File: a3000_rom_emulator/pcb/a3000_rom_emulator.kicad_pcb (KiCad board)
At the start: 4 copper layers, 43.2 x 78.7 mm, 43 parts

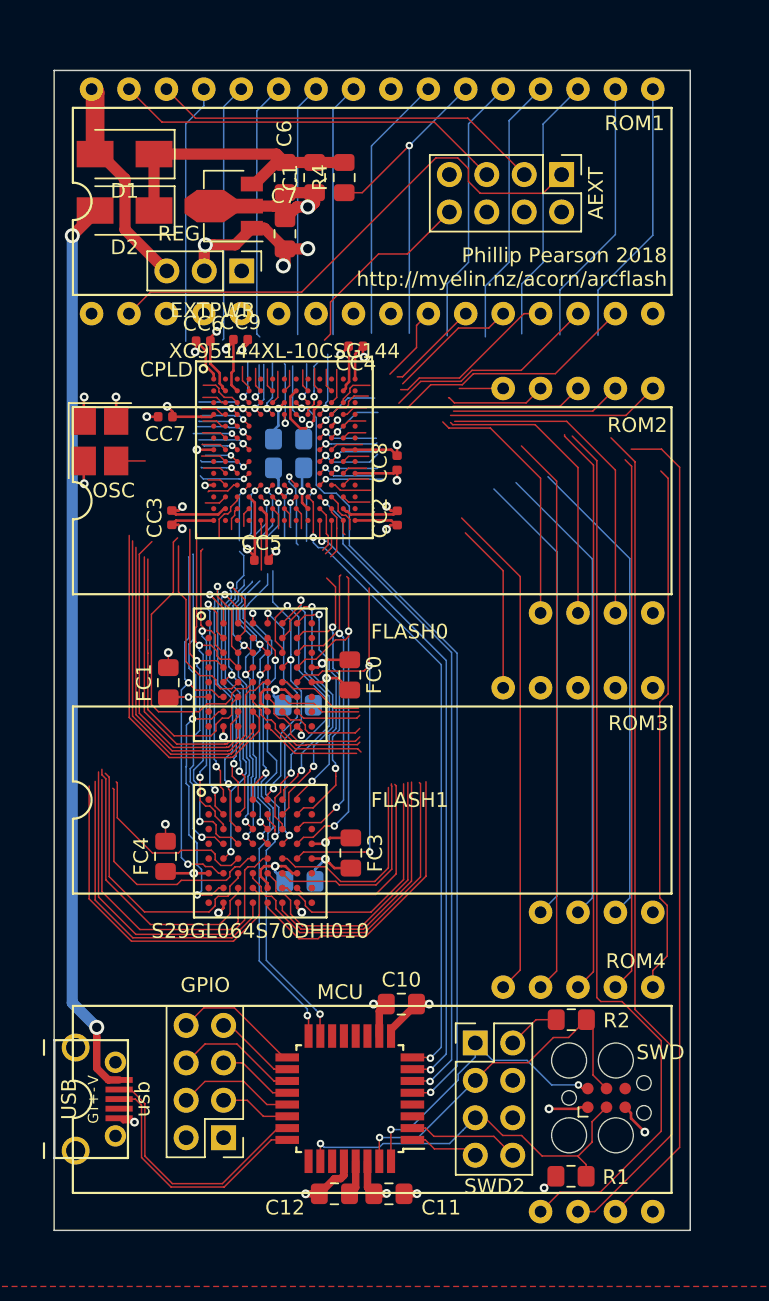
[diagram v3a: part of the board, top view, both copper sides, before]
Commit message: CPLD partially routed
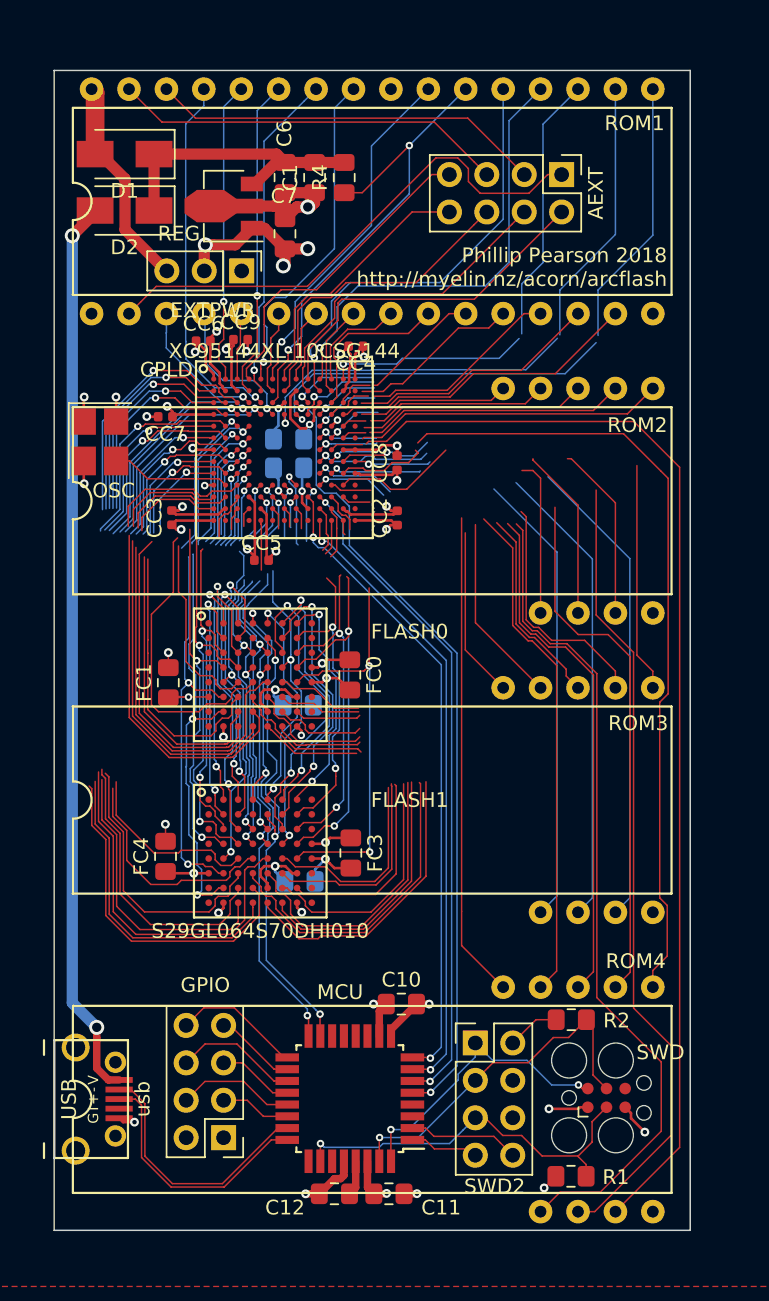
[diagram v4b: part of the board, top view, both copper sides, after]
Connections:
- CPLD pad A10: dummy_A10 -> rom_D6
- CPLD pad A11: dummy_A11 -> rom_A3
- CPLD pad A2: arc_RESET -> rom_A13
- CPLD pad A3: dummy_A3 -> rom_A7
- CPLD pad A4: dummy_A4 -> rom_A19
- CPLD pad A5: dummy_A5 -> rom_A11
- CPLD pad A6: dummy_A6 -> rom_A10
- CPLD pad A7: dummy_A7 -> arc_RESET
- CPLD pad A8: dummy_A8 -> rom_A5
- CPLD pad A9: dummy_A9 -> rom_A16
- CPLD pad B10: dummy_B10 -> rom_D7
- CPLD pad B11: dummy_B11 -> rom_A4
- CPLD pad B4: dummy_B4 -> rom_A8
- CPLD pad B5: dummy_B5 -> rom_A9
- CPLD pad B6: dummy_B6 -> rom_A6
- CPLD pad B7: dummy_B7 -> rom_A18
- CPLD pad B9: dummy_B9 -> rom_A17
- CPLD pad C11: dummy_C11 -> rom_A2
- CPLD pad C4: dummy_C4 -> rom_A15
- CPLD pad C5: dummy_C5 -> rom_A14
- CPLD pad C6: dummy_C6 -> rom_nCS
- CPLD pad D6: dummy_D6 -> rom_A12
- CPLD pad K2: dummy_K2_GCK1 -> osc_output
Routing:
- net rom_A16: track 0.00 -> 23.7 mm
- net rom_A17: track 0.00 -> 22.5 mm
- net rom_A19: track 0.00 -> 21.8 mm
- net rom_A18: track 0.00 -> 21.4 mm
- net dummy_D8: track 4.45 -> 24.5 mm
- net rom_D26: track 56.1 -> 75.5 mm
- net dummy_D7: track 4.69 -> 22.5 mm
- net rom_D27: track 36.1 -> 53.9 mm
- net rom_D20: track 0.00 -> 16.1 mm
- net rom_D19: track 0.00 -> 15.5 mm
- net dummy_B1: track 0.00 -> 14.8 mm, vias 0 -> 1
- net dummy_C3: track 2.94 -> 17.6 mm, vias 0 -> 1
- net rom_D21: track 0.00 -> 13.7 mm
- net dummy_A12: track 0.00 -> 13.7 mm, vias 0 -> 1
- net dummy_C1: track 0.00 -> 13.7 mm, vias 0 -> 1
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
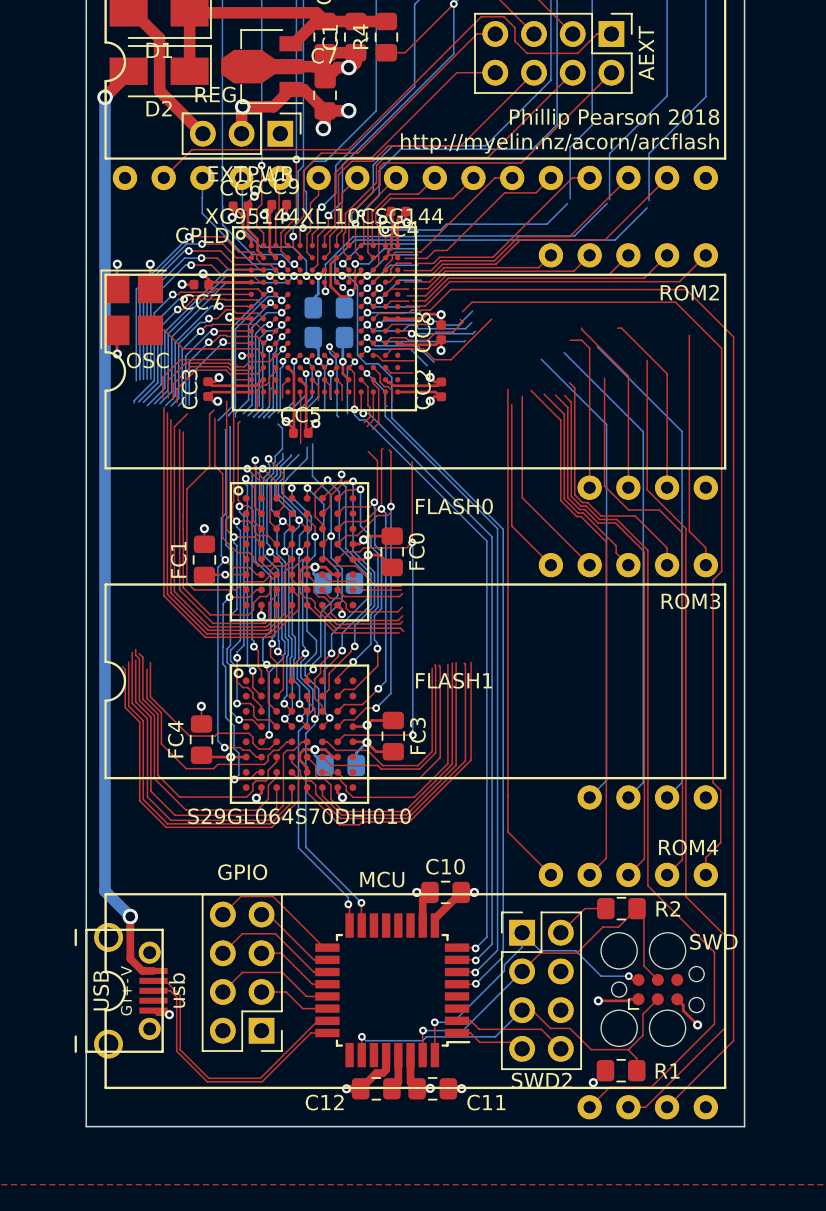
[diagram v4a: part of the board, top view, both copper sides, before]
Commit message: Fully routed PCB (still needs tidying) and basic Verilog for a3000_rom_emulator
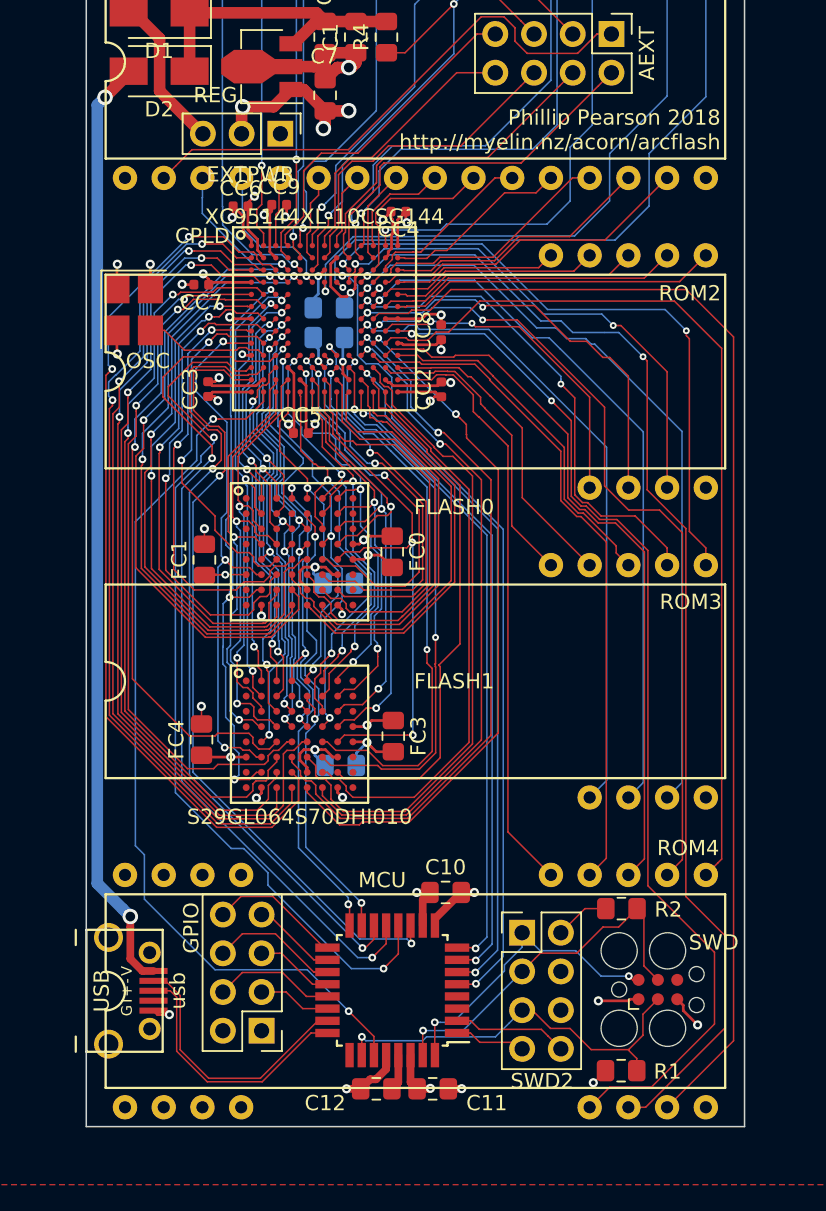
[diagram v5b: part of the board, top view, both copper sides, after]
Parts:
- added mech_pin1: , myelin-kicad:dip_rom_single_pin, F.Cu at (142.2, 91.4)
- added mech_pin2: , myelin-kicad:dip_rom_single_pin, F.Cu at (144.8, 91.4)
- added mech_pin3: , myelin-kicad:dip_rom_single_pin, F.Cu at (147.3, 91.4)
- added mech_pin4: , myelin-kicad:dip_rom_single_pin, F.Cu at (149.9, 91.4)
- added mech_pin5: , myelin-kicad:dip_rom_single_pin, F.Cu at (142.2, 106.7)
- added mech_pin6: , myelin-kicad:dip_rom_single_pin, F.Cu at (144.8, 106.7)
- added mech_pin7: , myelin-kicad:dip_rom_single_pin, F.Cu at (147.3, 106.7)
- added mech_pin8: , myelin-kicad:dip_rom_single_pin, F.Cu at (149.9, 106.7)
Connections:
- net osc_output renamed cpld_clock_osc
- CPLD pad A12: dummy_A12 -> rom_D5
- CPLD pad B1: dummy_B1 -> flash1_DQ3
- CPLD pad B13: dummy_B13 -> rom_A0
- CPLD pad C1: dummy_C1 -> flash1_DQ1
- CPLD pad C12: dummy_C12 -> rom_A1
- CPLD pad C13: dummy_C13 -> rom_D1
- CPLD pad C2: dummy_C2 -> flash1_DQ5
- CPLD pad C3: dummy_C3 -> flash1_DQ11
- CPLD pad C9: dummy_C9 -> rom_D19
- CPLD pad D10: dummy_D10 -> rom_D25
- CPLD pad D11: dummy_D11 -> rom_D0
- CPLD pad D12: dummy_D12 -> rom_D2
- CPLD pad D13: dummy_D13 -> rom_D15
- CPLD pad D2: dummy_D2 -> flash1_DQ9
- CPLD pad D3: dummy_D3 -> flash0_DQ3
- CPLD pad D4: dummy_D4 -> flash0_DQ11
- CPLD pad D5: dummy_D5 -> flash0_DQ5
- CPLD pad D7: dummy_D7 -> rom_D4
- CPLD pad D8: dummy_D8 -> rom_D3
- CPLD pad D9: dummy_D9 -> rom_D10
- CPLD pad E1: dummy_E1 -> flash1_DQ2
- CPLD pad E10: dummy_E10 -> rom_D18
- CPLD pad E12: dummy_E12 -> rom_D14
- CPLD pad E13: dummy_E13 -> rom_D13
- CPLD pad E2: dummy_E2 -> flash1_DQ8
- CPLD pad E3: dummy_E3 -> flash_nOE
- CPLD pad E4: dummy_E4 -> flash_A4
- CPLD pad F1: dummy_F1 -> flash0_DQ1
- CPLD pad F10: dummy_F10 -> rom_D20
- CPLD pad F11: dummy_F11 -> rom_D17
- CPLD pad F12: dummy_F12 -> rom_D12
- CPLD pad F13: dummy_F13 -> rom_D11
- CPLD pad F2: dummy_F2 -> flash1_DQ0
- CPLD pad F3: dummy_F3 -> flash_A3
- CPLD pad F4: dummy_F4 -> flash_A6
- CPLD pad G10: dummy_G10 -> rom_D9
- CPLD pad G11: dummy_G11 -> rom_D26
- CPLD pad G2: dummy_G2 -> flash0_DQ9
- CPLD pad G3: dummy_G3 -> flash_A7
- CPLD pad G4: dummy_G4 -> flash_A0
- CPLD pad H1: dummy_H1 -> flash0_DQ2
- CPLD pad H10: dummy_H10 -> rom_D16
- CPLD pad H11: dummy_H11 -> rom_D28
- CPLD pad H12: dummy_H12 -> rom_D8
- CPLD pad H13: dummy_H13 -> rom_D24
- CPLD pad H2: dummy_H2 -> flash0_DQ8
- CPLD pad H3: dummy_H3 -> flash_A18
- CPLD pad H4: dummy_H4 -> flash_A21
- CPLD pad J1: dummy_J1 -> flash_nCE
- CPLD pad J10: dummy_J10 -> flash1_DQ10
- CPLD pad J11: dummy_J11 -> flash1_DQ4
- CPLD pad J12: dummy_J12 -> rom_D27
- CPLD pad J2: dummy_J2 -> flash0_DQ0
- CPLD pad J3: dummy_J3 -> flash_A20
- CPLD pad J4: dummy_J4 -> flash_A19
- CPLD pad K10: dummy_K10 -> flash1_DQ6
- CPLD pad K11: dummy_K11 -> rom_D30
- CPLD pad K12: dummy_K12 -> rom_D29
- CPLD pad K13: dummy_K13 -> rom_D21
- CPLD pad K3: dummy_K3 -> cpld_SS
- CPLD pad K4: dummy_K4 -> flash_A11
- CPLD pad K5: dummy_K5 -> flash_A9
- CPLD pad K6: dummy_K6 -> flash_A14
- CPLD pad K7: dummy_K7 -> flash0_DQ14
- CPLD pad K8: dummy_K8 -> flash1_DQ7
- CPLD pad K9: dummy_K9 -> flash1_DQ14
- CPLD pad L1: dummy_L1_GCK2 -> cpld_SCK
- CPLD pad L11: dummy_L11 -> flash1_DQ12
- CPLD pad L12: dummy_L12 -> rom_D23
- CPLD pad L13: dummy_L13 -> rom_D22
- CPLD pad L2: dummy_L2 -> cpld_MISO
- CPLD pad L3: dummy_L3 -> flash_A17
- CPLD pad L5: dummy_L5 -> flash_A13
- CPLD pad L6: dummy_L6 -> flash0_DQ7
- CPLD pad L8: dummy_L8 -> flash0_DQ15
- CPLD pad M1: dummy_M1 -> cpld_MOSI
- CPLD pad M10: dummy_M10 -> flash0_DQ10
- CPLD pad M11: dummy_M11 -> flash1_DQ15
- CPLD pad M13: dummy_M13 -> rom_D31
- CPLD pad M3: dummy_M3 -> flash_A1
- CPLD pad M4: dummy_M4 -> flash_A2
- CPLD pad M6: dummy_M6 -> flash_A12
- CPLD pad M7: dummy_M7 -> flash_A16
- CPLD pad M8: dummy_M8 -> flash0_DQ12
- CPLD pad N11: dummy_N11 -> flash0_DQ4
- CPLD pad N12: dummy_N12 -> flash1_DQ13
- CPLD pad N2: dummy_N2_GCK3 -> cpld_clock_from_mcu
- CPLD pad N3: dummy_N3 -> flash_A5
- CPLD pad N4: dummy_N4 -> flash_nWE
- CPLD pad N5: dummy_N5 -> flash_A10
- CPLD pad N6: dummy_N6 -> flash_A8
- CPLD pad N7: dummy_N7 -> flash_A15
- CPLD pad N8: dummy_N8 -> flash0_DQ13
- CPLD pad N9: dummy_N9 -> flash0_DQ6
- MCU pad 27: (no net) -> cpld_clock_from_mcu
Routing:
- net cpld_clock_from_mcu: track 0.00 -> 58.3 mm, vias 0 -> 2
- net cpld_SCK: track 0.00 -> 57.6 mm, vias 0 -> 2
- net cpld_SS: track 0.00 -> 56.7 mm, vias 0 -> 2
- net cpld_MOSI: track 0.00 -> 52.6 mm, vias 0 -> 2
- net cpld_MISO: track 0.00 -> 51.9 mm, vias 0 -> 2
- net flash1_DQ11: track 23.2 -> 59.1 mm, vias 0 -> 2
- net flash1_DQ3: track 21.4 -> 54.3 mm, vias 0 -> 2
- net flash1_DQ5: track 25.1 -> 57.7 mm, vias 0 -> 2
- net flash1_DQ1: track 19.4 -> 51.1 mm, vias 0 -> 2
- net flash1_DQ9: track 19.6 -> 51.2 mm, vias 0 -> 2
- net flash1_DQ2: track 15.5 -> 46.4 mm, vias 0 -> 2
- net flash1_DQ0: track 12.5 -> 43.5 mm, vias 0 -> 2
- net flash1_DQ8: track 18.7 -> 49.1 mm, vias 0 -> 2
- net rom_D19: track 15.5 -> 41.9 mm, vias 0 -> 2
- net flash1_DQ10: track 21.8 -> 48.0 mm, vias 0 -> 2
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
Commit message: Tidy up some traces
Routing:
- net rom_D7: track 29.7 -> 26.2 mm
- net rom_D6: track 31.1 -> 28.5 mm
- net rom_D25: track 76.8 -> 74.7 mm
- net flash1_DQ4: track 45.9 -> 44.0 mm
- net cpld_MOSI: track 52.6 -> 50.8 mm
- net flash1_DQ10: track 48.0 -> 46.3 mm
- net rom_D10: track 33.2 -> 31.6 mm
- net cpld_SCK: track 57.6 -> 56.2 mm
- net flash1_DQ6: track 43.2 -> 41.8 mm
- net rom_D18: track 50.8 -> 49.4 mm
- net flash1_DQ12: track 43.0 -> 41.7 mm
- net rom_D9: track 27.4 -> 26.1 mm
- net flash0_DQ10: track 29.9 -> 29.0 mm
- net flash1_DQ15: track 35.5 -> 34.6 mm
- net flash0_DQ13: track 25.5 -> 24.5 mm
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
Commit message: More tidying, plus added 30 ground staples, and removed some spurious lines from constraints.ucf
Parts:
- added staple_single1: , myelin-kicad:via_single, F.Cu at (168.0, 33.9)
- added staple_single10: , myelin-kicad:via_single, F.Cu at (143.5, 48.7)
- added staple_single11: , myelin-kicad:via_single, F.Cu at (176.6, 33.0)
- added staple_single12: , myelin-kicad:via_single, F.Cu at (173.0, 43.6)
- added staple_single13: , myelin-kicad:via_single, F.Cu at (179.1, 33.0)
- added staple_single14: , myelin-kicad:via_single, F.Cu at (181.6, 33.0)
- added staple_single15: , myelin-kicad:via_single, F.Cu at (176.0, 43.5)
- added staple_single16: , myelin-kicad:via_single, F.Cu at (160.2, 33.8)
- added staple_single17: , myelin-kicad:via_single, F.Cu at (162.4, 34.3)
- added staple_single18: , myelin-kicad:via_single, F.Cu at (165.3, 34.1)
- added staple_single19: , myelin-kicad:via_single, F.Cu at (163.9, 41.4)
- added staple_single2: , myelin-kicad:via_single, F.Cu at (175.2, 84.2)
- added staple_single20: , myelin-kicad:via_single, F.Cu at (150.0, 33.6)
- added staple_single21: , myelin-kicad:via_single, F.Cu at (150.3, 36.1)
- added staple_single22: , myelin-kicad:via_single, F.Cu at (147.5, 40.7)
- added staple_single23: , myelin-kicad:via_single, F.Cu at (142.3, 88.5)
- added staple_single24: , myelin-kicad:via_single, F.Cu at (156.6, 55.2)
- added staple_single25: , myelin-kicad:via_single, F.Cu at (144.5, 74.5)
- added staple_single26: , myelin-kicad:via_single, F.Cu at (144.6, 78.8)
- added staple_single27: , myelin-kicad:via_single, F.Cu at (147.3, 76.9)
- added staple_single28: , myelin-kicad:via_single, F.Cu at (173.6, 55.4)
- added staple_single29: , myelin-kicad:via_single, F.Cu at (180.2, 57.7)
- added staple_single3: , myelin-kicad:via_single, F.Cu at (175.2, 73.5)
- added staple_single30: , myelin-kicad:via_single, F.Cu at (170.9, 84.2)
- added staple_single4: , myelin-kicad:via_single, F.Cu at (177.8, 84.2)
- added staple_single5: , myelin-kicad:via_single, F.Cu at (177.8, 75.4)
- added staple_single6: , myelin-kicad:via_single, F.Cu at (180.4, 75.4)
- added staple_single7: , myelin-kicad:via_single, F.Cu at (180.4, 84.2)
- added staple_single8: , myelin-kicad:via_single, F.Cu at (160.1, 100.0)
- added staple_single9: , myelin-kicad:via_single, F.Cu at (144.7, 32.6)
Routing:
- net rom_D19: track 41.9 -> 40.0 mm
- net cpld_MOSI: track 50.8 -> 52.0 mm

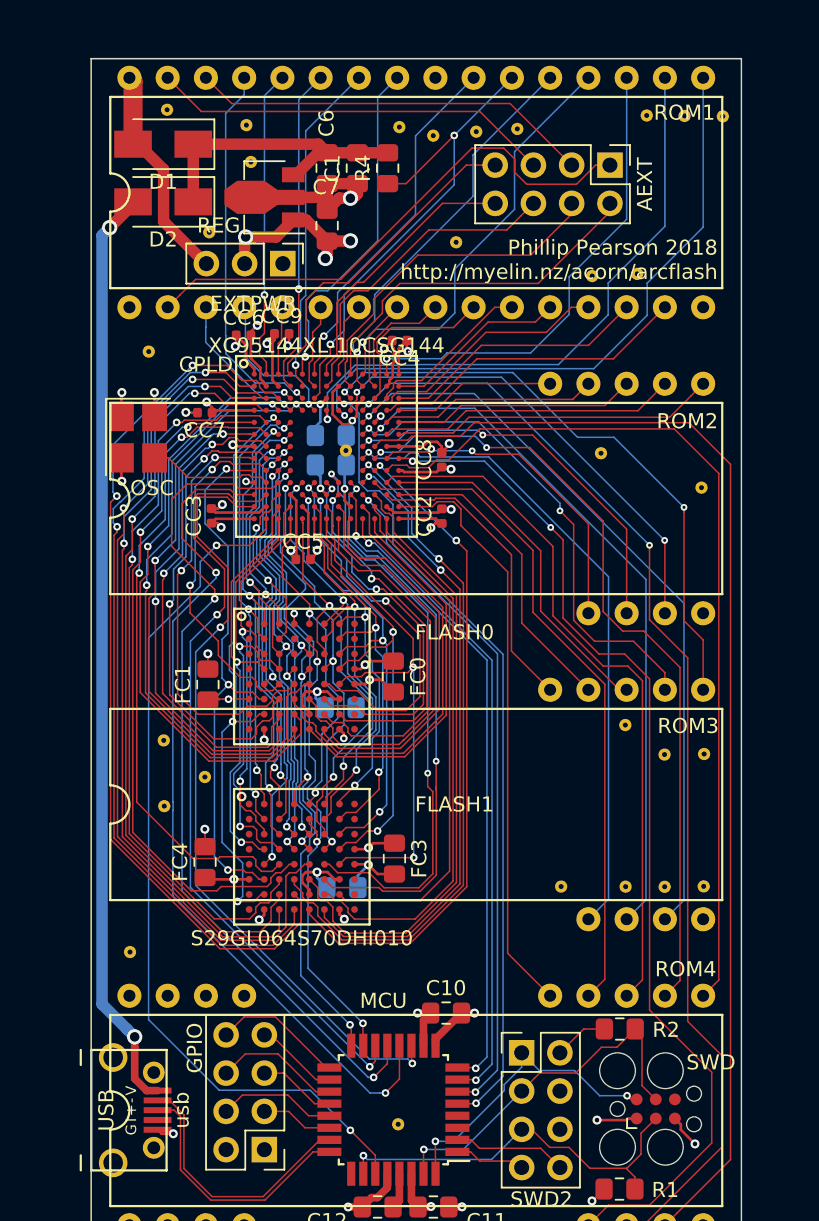
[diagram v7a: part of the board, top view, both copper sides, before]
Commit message: Silkscreen, some tracks
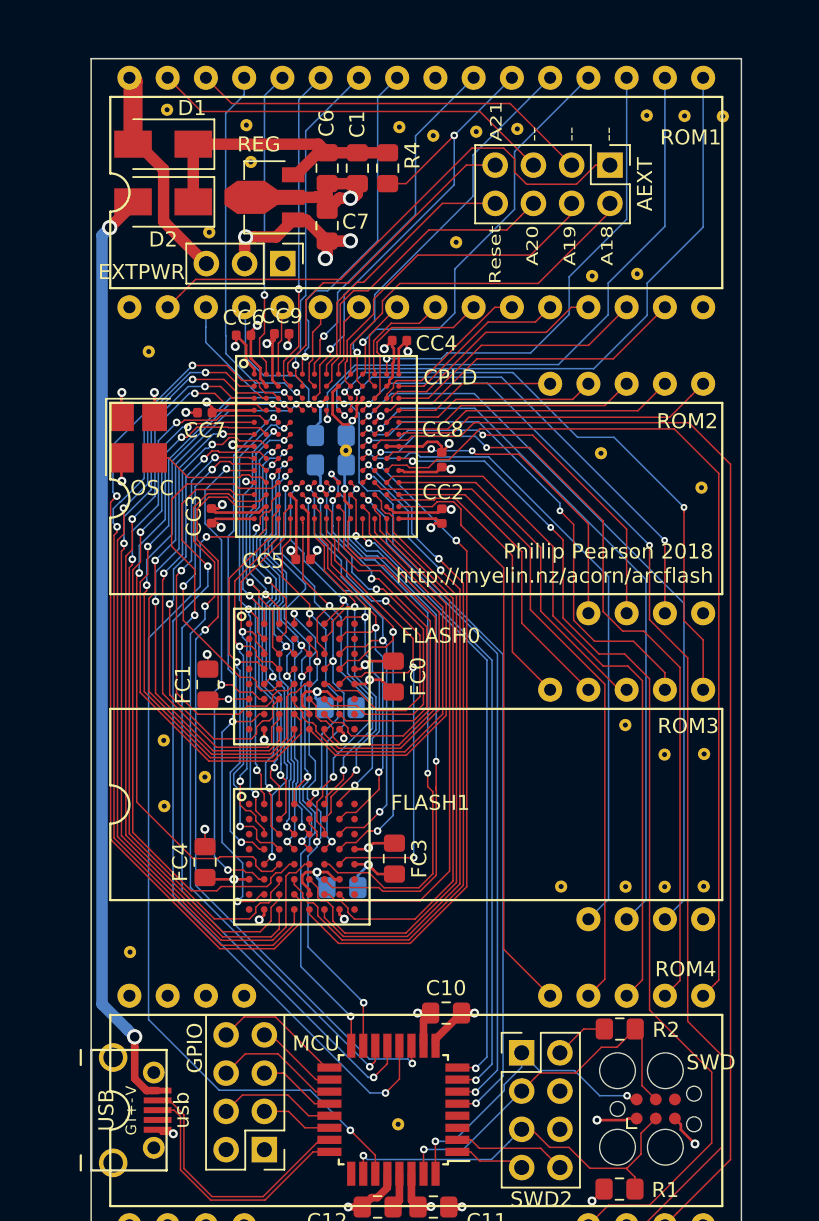
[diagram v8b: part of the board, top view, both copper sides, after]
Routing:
- net cpld_SS: track 56.2 -> 55.1 mm
- net cpld_MISO: track 51.4 -> 50.5 mm
- net cpld_MOSI: track 52.0 -> 51.1 mm
- net cpld_clock_from_mcu: track 57.8 -> 58.5 mm
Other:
- board text added: "A21 -- -- --"
- board text added: "Reset A20 A19 A18"
